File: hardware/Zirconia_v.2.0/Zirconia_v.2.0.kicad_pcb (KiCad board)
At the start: 2 copper layers, 39 x 91 mm, 91 parts, among them J1 BD125-10-A-0305-0580-L-B, J2 Conn_01x04, J4 BD125-10-A-0305-0580-L-B, P1 Red, P2 Blk, P3 Red, P4 Blk, P6 PicoBlade_53047-0210, Q1 LTR, Q2 LTR, Q3 LTR, Q4 LTR, Q5 IRLML6344, Q6 IRLML6344, Q7 IRLML6344, Q8 IRLML6344, Q9 DMC2400UV-7, SW1 KMR211NG LFS, SW2 SS12D01G4, U1 MA302/MA730, U10 ENCODER_CONNECT_IC, U11 LP5907MFX-3.0, U12 STLINK-V3MOS, U2 ENCODER_CONNECT_IC, U3 DRV8836DSSR, U4 STM32F411CEU6/STM32F413CHU6, U5 ENCODER_CONNECT_PCB, U6 ENCODER_CONNECT_PCB, U7 MCP73831T-2ACI/OT, U8 ICM-42688-P, U9 MA302/MA730

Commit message: update
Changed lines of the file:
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@@
 		(fp_arc
 			(start 0.29 5.07)
-			(mid -1.269999 6.629999)
+			(mid -1.270001 6.63)
 			(end -2.83 5.07)
 			(stroke
@@
 		(fp_arc
 			(start 0.23 5.07)
-			(mid -1.27 6.569999)
+			(mid -1.27 6.57)
 			(end -2.77 5.07)
 			(stroke
@@
 		(fp_arc
 			(start 2.83 5.07)
-			(mid 1.27 6.629999)
+			(mid 1.27 6.629998)
 			(end -0.290001 5.07)
 			(stroke

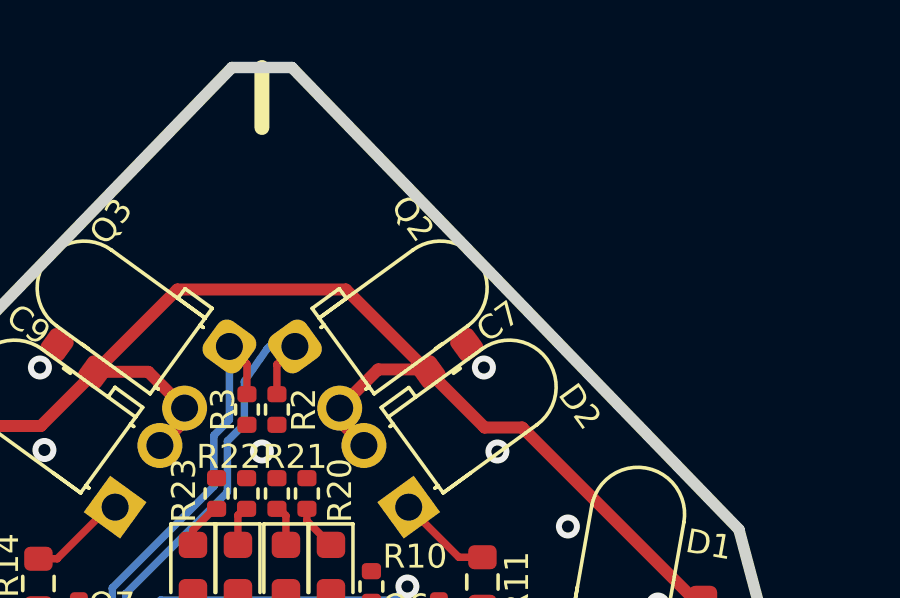
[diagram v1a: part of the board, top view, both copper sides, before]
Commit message: JLCPCBパーツ反映
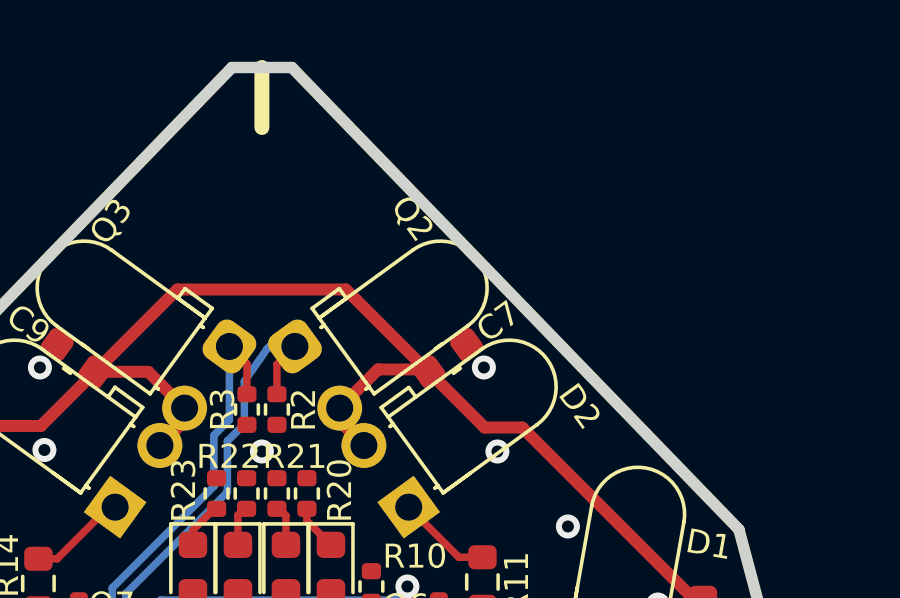
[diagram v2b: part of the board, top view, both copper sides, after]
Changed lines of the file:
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@@
 		(fp_arc
 			(start 0.29 5.07)
-			(mid -1.270001 6.63)
+			(mid -1.269999 6.629999)
 			(end -2.83 5.07)
 			(stroke
@@
 		(fp_arc
 			(start 0.23 5.07)
-			(mid -1.27 6.57)
+			(mid -1.27 6.569999)
 			(end -2.77 5.07)
 			(stroke
@@
 		(fp_arc
 			(start 2.83 5.07)
-			(mid 1.27 6.629998)
+			(mid 1.269998 6.629999)
 			(end -0.290001 5.07)
 			(stroke
